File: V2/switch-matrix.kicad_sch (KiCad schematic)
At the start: 256 parts

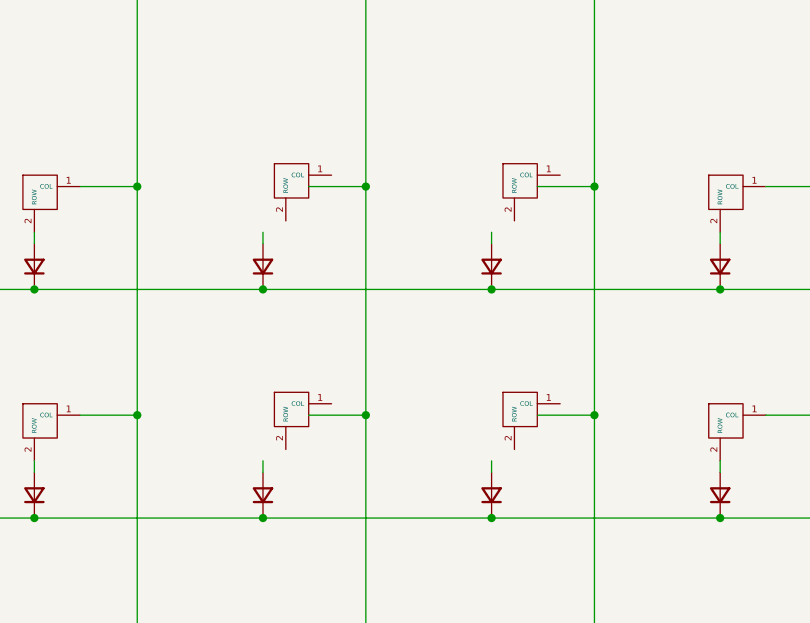
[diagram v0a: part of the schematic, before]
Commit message: Fixes + new files
Added RP2040 docs, fixed diodes in key matrix schematic, assigned RP2040 footprint to KiCAD stock QFN-56 7x7 package and made the BOOTSEL and RESET buttons smaller format.
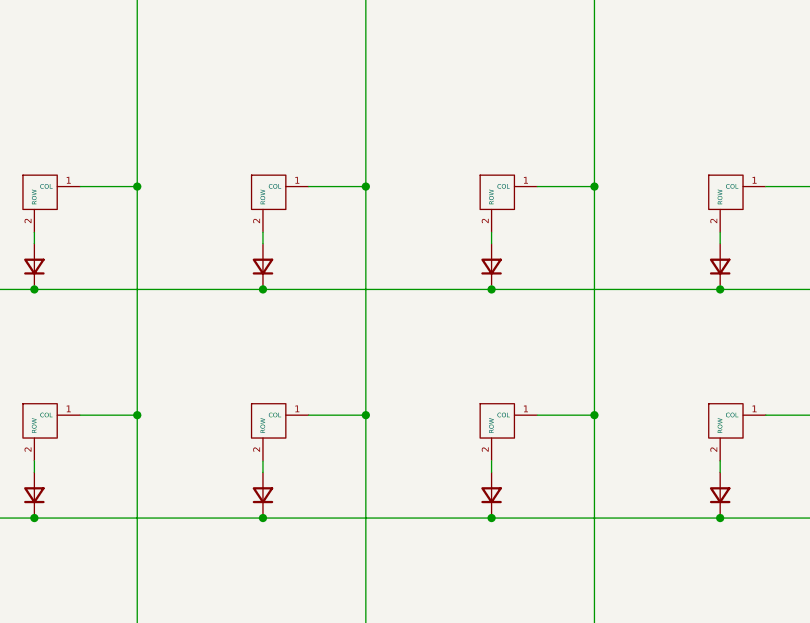
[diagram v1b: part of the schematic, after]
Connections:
- net col14: now also K_92.1 (COL), K_93.1 (COL)
- net col15: now also K_98.1 (COL), K_99.1 (COL)
- net at D_92.2 (A): now also K_92.2 (ROW)
- net at D_98.2 (A): now also K_98.2 (ROW)
- net at D_93.2 (A): now also K_93.2 (ROW)
- net at D_99.2 (A): now also K_99.2 (ROW)
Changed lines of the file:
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@@
 	)
 	(junction
+		(at 445.77 139.7)
+		(diameter 0)
+		(color 0 0 0 0)
+	)
+	(junction
 		(at 344.17 63.5)
 		(diameter 0)
@@
 	)
 	(junction
-		(at 445.77 139.7)
-		(diameter 0)
-		(color 0 0 0 0)
-	)
-	(junction
 		(at 535.94 74.93)
 		(diameter 0)
@@
 	(symbol
 		(lib_id "122-LIB:MX_Kailh_Hotswap_PnP")
-		(at 435.61 115.57 0)
+		(at 433.07 116.84 0)
 		(unit 1)
 		(body_style 1)
@@
 		(dnp no)
 		(property "Reference" "K_92"
-			(at 435.61 109.6518 0)
+			(at 433.07 110.9218 0)
 			(hide yes)
 			(show_name no)
@@
 		)
 		(property "Value" "KEYSW"
-			(at 435.61 118.11 0)
+			(at 433.07 119.38 0)
 			(hide yes)
 			(show_name no)
@@
 		)
 		(property "Footprint" "122-LIB:SW_Hotswap_Kailh_MX_1.00u_PnP"
-			(at 435.61 115.57 0)
+			(at 433.07 116.84 0)
 			(hide yes)
 			(show_name no)
@@
 		)
 		(property "Datasheet" ""
-			(at 435.61 115.57 0)
+			(at 433.07 116.84 0)
 			(hide yes)
 			(show_name no)
@@
 		)
 		(property "Description" ""
-			(at 435.61 115.57 0)
+			(at 433.07 116.84 0)
 			(hide yes)
 			(show_name no)
@@
 	(symbol
 		(lib_id "122-LIB:MX_Kailh_Hotswap_PnP")
-		(at 461.01 115.57 0)
+		(at 458.47 116.84 0)
 		(unit 1)
 		(body_style 1)
@@
 		(dnp no)
 		(property "Reference" "K_98"
-			(at 461.01 109.6518 0)
+			(at 458.47 110.9218 0)
 			(hide yes)
 			(show_name no)
@@
 		)
 		(property "Value" "KEYSW"
-			(at 461.01 118.11 0)
+			(at 458.47 119.38 0)
 			(hide yes)
 			(show_name no)
@@
 		)
 		(property "Footprint" "122-LIB:SW_Hotswap_Kailh_MX_1.00u_PnP"
-			(at 461.01 115.57 0)
+			(at 458.47 116.84 0)
 			(hide yes)
 			(show_name no)
@@
 		)
 		(property "Datasheet" ""
-			(at 461.01 115.57 0)
+			(at 458.47 116.84 0)
 			(hide yes)
 			(show_name no)
@@
 		)
 		(property "Description" ""
-			(at 461.01 115.57 0)
+			(at 458.47 116.84 0)
 			(hide yes)
 			(show_name no)
@@
 	(symbol
 		(lib_id "122-LIB:MX_Kailh_Hotswap_PnP")
-		(at 435.61 140.97 0)
+		(at 433.07 142.24 0)
 		(unit 1)
 		(body_style 1)
@@
 		(dnp no)
 		(property "Reference" "K_93"
-			(at 435.61 135.0518 0)
+			(at 433.07 136.3218 0)
 			(hide yes)
 			(show_name no)
@@
 		)
 		(property "Value" "KEYSW"
-			(at 435.61 143.51 0)
+			(at 433.07 144.78 0)
 			(hide yes)
 			(show_name no)
@@
 		)
 		(property "Footprint" "122-LIB:SW_Hotswap_Kailh_MX_1.00u_PnP"
-			(at 435.61 140.97 0)
+			(at 433.07 142.24 0)
 			(hide yes)
 			(show_name no)
@@
 		)
 		(property "Datasheet" ""
-			(at 435.61 140.97 0)
+			(at 433.07 142.24 0)
 			(hide yes)
 			(show_name no)
@@
 		)
 		(property "Description" ""
-			(at 435.61 140.97 0)
+			(at 433.07 142.24 0)
 			(hide yes)
 			(show_name no)
@@
 	(symbol
 		(lib_id "122-LIB:MX_Kailh_Hotswap_PnP")
-		(at 461.01 140.97 0)
+		(at 458.47 142.24 0)
 		(unit 1)
 		(body_style 1)
@@
 		(dnp no)
 		(property "Reference" "K_99"
-			(at 461.01 135.0518 0)
+			(at 458.47 136.3218 0)
 			(hide yes)
 			(show_name no)
@@
 		)
 		(property "Value" "KEYSW"
-			(at 461.01 143.51 0)
+			(at 458.47 144.78 0)
 			(hide yes)
 			(show_name no)
@@
 		)
 		(property "Footprint" "122-LIB:SW_Hotswap_Kailh_MX_1.00u_PnP"
-			(at 461.01 140.97 0)
+			(at 458.47 142.24 0)
 			(hide yes)
 			(show_name no)
@@
 		)
 		(property "Datasheet" ""
-			(at 461.01 140.97 0)
+			(at 458.47 142.24 0)
 			(hide yes)
 			(show_name no)
@@
 		)
 		(property "Description" ""
-			(at 461.01 140.97 0)
+			(at 458.47 142.24 0)
 			(hide yes)
 			(show_name no)

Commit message: Added PnP for plated thru holes + literature
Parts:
- K_1, K_128, K_94: footprint 122-LIB:SW_Hotswap_Kailh_MX_1.00u_PnP -> 122-LIB:SW_Hotswap_Kailh_MX_Plated_1.00u_PnP
- K_10: renamed from K_64; footprint 122-LIB:SW_Hotswap_Kailh_MX_1.00u_PnP -> 122-LIB:SW_Hotswap_Kailh_MX_Plated_1.00u_PnP
- K_100: renamed from K_5; footprint 122-LIB:SW_Hotswap_Kailh_MX_1.00u_PnP -> 122-LIB:SW_Hotswap_Kailh_MX_Plated_1.00u_PnP
- K_101: renamed from K_10; footprint 122-LIB:SW_Hotswap_Kailh_MX_1.00u_PnP -> 122-LIB:SW_Hotswap_Kailh_MX_Plated_1.00u_PnP
- K_102: renamed from K_16; footprint 122-LIB:SW_Hotswap_Kailh_MX_1.00u_PnP -> 122-LIB:SW_Hotswap_Kailh_MX_Plated_1.00u_PnP
- K_103: renamed from K_23; footprint 122-LIB:SW_Hotswap_Kailh_MX_1.00u_PnP -> 122-LIB:SW_Hotswap_Kailh_MX_Plated_1.00u_PnP
- K_104: renamed from K_29; footprint 122-LIB:SW_Hotswap_Kailh_MX_1.00u_PnP -> 122-LIB:SW_Hotswap_Kailh_MX_Plated_1.00u_PnP
- K_105: renamed from K_36; footprint 122-LIB:SW_Hotswap_Kailh_MX_1.00u_PnP -> 122-LIB:SW_Hotswap_Kailh_MX_Plated_1.00u_PnP
- K_106: renamed from K_43; footprint 122-LIB:SW_Hotswap_Kailh_MX_1.00u_PnP -> 122-LIB:SW_Hotswap_Kailh_MX_Plated_1.00u_PnP
- K_107: renamed from K_50; footprint 122-LIB:SW_Hotswap_Kailh_MX_1.00u_PnP -> 122-LIB:SW_Hotswap_Kailh_MX_Plated_1.00u_PnP
- K_108: renamed from K_57; footprint 122-LIB:SW_Hotswap_Kailh_MX_1.00u_PnP -> 122-LIB:SW_Hotswap_Kailh_MX_Plated_1.00u_PnP
- K_109: renamed from K_63; footprint 122-LIB:SW_Hotswap_Kailh_MX_1.00u_PnP -> 122-LIB:SW_Hotswap_Kailh_MX_Plated_1.00u_PnP
- K_11: renamed from K_71; footprint 122-LIB:SW_Hotswap_Kailh_MX_1.00u_PnP -> 122-LIB:SW_Hotswap_Kailh_MX_Plated_1.00u_PnP
- K_110: renamed from K_69; footprint 122-LIB:SW_Hotswap_Kailh_MX_1.00u_PnP -> 122-LIB:SW_Hotswap_Kailh_MX_Plated_1.00u_PnP
- K_111: renamed from K_76; footprint 122-LIB:SW_Hotswap_Kailh_MX_1.00u_PnP -> 122-LIB:SW_Hotswap_Kailh_MX_Plated_1.00u_PnP
- K_112: renamed from K_82; footprint 122-LIB:SW_Hotswap_Kailh_MX_1.00u_PnP -> 122-LIB:SW_Hotswap_Kailh_MX_Plated_1.00u_PnP
- K_113: renamed from K_88; footprint 122-LIB:SW_Hotswap_Kailh_MX_1.00u_PnP -> 122-LIB:SW_Hotswap_Kailh_MX_Plated_1.00u_PnP
- K_114: renamed from K_95; footprint 122-LIB:SW_Hotswap_Kailh_MX_1.00u_PnP -> 122-LIB:SW_Hotswap_Kailh_MX_Plated_1.00u_PnP
- K_115: renamed from K_101; footprint 122-LIB:SW_Hotswap_Kailh_MX_1.00u_PnP -> 122-LIB:SW_Hotswap_Kailh_MX_Plated_1.00u_PnP
- K_116: renamed from K_117; footprint 122-LIB:SW_Hotswap_Kailh_MX_1.00u_PnP -> 122-LIB:SW_Hotswap_Kailh_MX_Plated_1.00u_PnP
- K_117: renamed from K_6; footprint 122-LIB:SW_Hotswap_Kailh_MX_1.00u_PnP -> 122-LIB:SW_Hotswap_Kailh_MX_Plated_1.00u_PnP
- K_118: renamed from K_17; footprint 122-LIB:SW_Hotswap_Kailh_MX_1.00u_PnP -> 122-LIB:SW_Hotswap_Kailh_MX_Plated_1.00u_PnP
- K_119: renamed from K_30; footprint 122-LIB:SW_Hotswap_Kailh_MX_1.00u_PnP -> 122-LIB:SW_Hotswap_Kailh_MX_Plated_1.00u_PnP
- K_12: renamed from K_77; footprint 122-LIB:SW_Hotswap_Kailh_MX_1.00u_PnP -> 122-LIB:SW_Hotswap_Kailh_MX_Plated_1.00u_PnP
- K_120: renamed from K_37; footprint 122-LIB:SW_Hotswap_Kailh_MX_1.00u_PnP -> 122-LIB:SW_Hotswap_Kailh_MX_Plated_1.00u_PnP
- K_121: renamed from K_44; footprint 122-LIB:SW_Hotswap_Kailh_MX_1.00u_PnP -> 122-LIB:SW_Hotswap_Kailh_MX_Plated_1.00u_PnP
- K_122: renamed from K_51; footprint 122-LIB:SW_Hotswap_Kailh_MX_1.00u_PnP -> 122-LIB:SW_Hotswap_Kailh_MX_Plated_1.00u_PnP
- K_123: renamed from K_70; footprint 122-LIB:SW_Hotswap_Kailh_MX_1.00u_PnP -> 122-LIB:SW_Hotswap_Kailh_MX_Plated_1.00u_PnP
- K_124: renamed from K_89; footprint 122-LIB:SW_Hotswap_Kailh_MX_1.00u_PnP -> 122-LIB:SW_Hotswap_Kailh_MX_Plated_1.00u_PnP
- K_125: renamed from K_102; footprint 122-LIB:SW_Hotswap_Kailh_MX_1.00u_PnP -> 122-LIB:SW_Hotswap_Kailh_MX_Plated_1.00u_PnP
- K_126: renamed from K_118; footprint 122-LIB:SW_Hotswap_Kailh_MX_1.00u_PnP -> 122-LIB:SW_Hotswap_Kailh_MX_Plated_1.00u_PnP
- K_127: renamed from K_124; footprint 122-LIB:SW_Hotswap_Kailh_MX_1.00u_PnP -> 122-LIB:SW_Hotswap_Kailh_MX_Plated_1.00u_PnP
- K_13: renamed from K_83; footprint 122-LIB:SW_Hotswap_Kailh_MX_1.00u_PnP -> 122-LIB:SW_Hotswap_Kailh_MX_Plated_1.00u_PnP
- K_14: renamed from K_90; footprint 122-LIB:SW_Hotswap_Kailh_MX_1.00u_PnP -> 122-LIB:SW_Hotswap_Kailh_MX_Plated_1.00u_PnP
- K_15: renamed from K_96; footprint 122-LIB:SW_Hotswap_Kailh_MX_1.00u_PnP -> 122-LIB:SW_Hotswap_Kailh_MX_Plated_1.00u_PnP
- K_16: renamed from K_103; footprint 122-LIB:SW_Hotswap_Kailh_MX_1.00u_PnP -> 122-LIB:SW_Hotswap_Kailh_MX_Plated_1.00u_PnP
- K_17: renamed from K_108; footprint 122-LIB:SW_Hotswap_Kailh_MX_1.00u_PnP -> 122-LIB:SW_Hotswap_Kailh_MX_Plated_1.00u_PnP
- K_18: renamed from K_112; footprint 122-LIB:SW_Hotswap_Kailh_MX_1.00u_PnP -> 122-LIB:SW_Hotswap_Kailh_MX_Plated_1.00u_PnP
- K_19: renamed from K_119; footprint 122-LIB:SW_Hotswap_Kailh_MX_1.00u_PnP -> 122-LIB:SW_Hotswap_Kailh_MX_Plated_1.00u_PnP
- K_2: renamed from K_11; footprint 122-LIB:SW_Hotswap_Kailh_MX_1.00u_PnP -> 122-LIB:SW_Hotswap_Kailh_MX_Plated_1.00u_PnP
- K_20: renamed from K_12; footprint 122-LIB:SW_Hotswap_Kailh_MX_1.00u_PnP -> 122-LIB:SW_Hotswap_Kailh_MX_Plated_1.00u_PnP
- K_21: renamed from K_19; footprint 122-LIB:SW_Hotswap_Kailh_MX_1.00u_PnP -> 122-LIB:SW_Hotswap_Kailh_MX_Plated_1.00u_PnP
- K_22: renamed from K_25; footprint 122-LIB:SW_Hotswap_Kailh_MX_1.00u_PnP -> 122-LIB:SW_Hotswap_Kailh_MX_Plated_1.00u_PnP
- K_23: renamed from K_32; footprint 122-LIB:SW_Hotswap_Kailh_MX_1.00u_PnP -> 122-LIB:SW_Hotswap_Kailh_MX_Plated_1.00u_PnP
- K_24: renamed from K_39; footprint 122-LIB:SW_Hotswap_Kailh_MX_1.00u_PnP -> 122-LIB:SW_Hotswap_Kailh_MX_Plated_1.00u_PnP
- K_25: renamed from K_46; footprint 122-LIB:SW_Hotswap_Kailh_MX_1.00u_PnP -> 122-LIB:SW_Hotswap_Kailh_MX_Plated_1.00u_PnP
- K_26: renamed from K_53; footprint 122-LIB:SW_Hotswap_Kailh_MX_1.00u_PnP -> 122-LIB:SW_Hotswap_Kailh_MX_Plated_1.00u_PnP
- K_27: renamed from K_59; footprint 122-LIB:SW_Hotswap_Kailh_MX_1.00u_PnP -> 122-LIB:SW_Hotswap_Kailh_MX_Plated_1.00u_PnP
- K_28: renamed from K_65; footprint 122-LIB:SW_Hotswap_Kailh_MX_1.00u_PnP -> 122-LIB:SW_Hotswap_Kailh_MX_Plated_1.00u_PnP
- K_29: renamed from K_72; footprint 122-LIB:SW_Hotswap_Kailh_MX_1.00u_PnP -> 122-LIB:SW_Hotswap_Kailh_MX_Plated_1.00u_PnP
- K_3: renamed from K_18; footprint 122-LIB:SW_Hotswap_Kailh_MX_1.00u_PnP -> 122-LIB:SW_Hotswap_Kailh_MX_Plated_1.00u_PnP
- K_30: renamed from K_78; footprint 122-LIB:SW_Hotswap_Kailh_MX_1.00u_PnP -> 122-LIB:SW_Hotswap_Kailh_MX_Plated_1.00u_PnP
- K_31: renamed from K_84; footprint 122-LIB:SW_Hotswap_Kailh_MX_1.00u_PnP -> 122-LIB:SW_Hotswap_Kailh_MX_Plated_1.00u_PnP
- K_32: renamed from K_91; footprint 122-LIB:SW_Hotswap_Kailh_MX_1.00u_PnP -> 122-LIB:SW_Hotswap_Kailh_MX_Plated_1.00u_PnP
- K_33: renamed from K_97; footprint 122-LIB:SW_Hotswap_Kailh_MX_1.00u_PnP -> 122-LIB:SW_Hotswap_Kailh_MX_Plated_1.00u_PnP
- K_34: renamed from K_104; footprint 122-LIB:SW_Hotswap_Kailh_MX_1.00u_PnP -> 122-LIB:SW_Hotswap_Kailh_MX_Plated_1.00u_PnP
- K_35: renamed from K_109; footprint 122-LIB:SW_Hotswap_Kailh_MX_1.00u_PnP -> 122-LIB:SW_Hotswap_Kailh_MX_Plated_1.00u_PnP
- K_36: renamed from K_113; footprint 122-LIB:SW_Hotswap_Kailh_MX_1.00u_PnP -> 122-LIB:SW_Hotswap_Kailh_MX_Plated_1.00u_PnP
- K_37: renamed from K_120; footprint 122-LIB:SW_Hotswap_Kailh_MX_1.00u_PnP -> 122-LIB:SW_Hotswap_Kailh_MX_Plated_1.00u_PnP
- K_38: renamed from K_2; footprint 122-LIB:SW_Hotswap_Kailh_MX_1.00u_PnP -> 122-LIB:SW_Hotswap_Kailh_MX_Plated_1.00u_PnP
- K_39: renamed from K_7; footprint 122-LIB:SW_Hotswap_Kailh_MX_1.00u_PnP -> 122-LIB:SW_Hotswap_Kailh_MX_Plated_1.00u_PnP
- K_4: renamed from K_24; footprint 122-LIB:SW_Hotswap_Kailh_MX_1.00u_PnP -> 122-LIB:SW_Hotswap_Kailh_MX_Plated_1.00u_PnP
- K_40: renamed from K_13; footprint 122-LIB:SW_Hotswap_Kailh_MX_1.00u_PnP -> 122-LIB:SW_Hotswap_Kailh_MX_Plated_1.00u_PnP
- K_41: renamed from K_20; footprint 122-LIB:SW_Hotswap_Kailh_MX_1.00u_PnP -> 122-LIB:SW_Hotswap_Kailh_MX_Plated_1.00u_PnP
- K_42: renamed from K_26; footprint 122-LIB:SW_Hotswap_Kailh_MX_1.00u_PnP -> 122-LIB:SW_Hotswap_Kailh_MX_Plated_1.00u_PnP
- K_43: renamed from K_33; footprint 122-LIB:SW_Hotswap_Kailh_MX_1.00u_PnP -> 122-LIB:SW_Hotswap_Kailh_MX_Plated_1.00u_PnP
- K_44: renamed from K_40; footprint 122-LIB:SW_Hotswap_Kailh_MX_1.00u_PnP -> 122-LIB:SW_Hotswap_Kailh_MX_Plated_1.00u_PnP
- K_45: renamed from K_47; footprint 122-LIB:SW_Hotswap_Kailh_MX_1.00u_PnP -> 122-LIB:SW_Hotswap_Kailh_MX_Plated_1.00u_PnP
- K_46: renamed from K_54; footprint 122-LIB:SW_Hotswap_Kailh_MX_1.00u_PnP -> 122-LIB:SW_Hotswap_Kailh_MX_Plated_1.00u_PnP
- K_47: renamed from K_60; footprint 122-LIB:SW_Hotswap_Kailh_MX_1.00u_PnP -> 122-LIB:SW_Hotswap_Kailh_MX_Plated_1.00u_PnP
- K_48: renamed from K_66; footprint 122-LIB:SW_Hotswap_Kailh_MX_1.00u_PnP -> 122-LIB:SW_Hotswap_Kailh_MX_Plated_1.00u_PnP
- K_49: renamed from K_73; footprint 122-LIB:SW_Hotswap_Kailh_MX_1.00u_PnP -> 122-LIB:SW_Hotswap_Kailh_MX_Plated_1.00u_PnP
- K_5: renamed from K_31; footprint 122-LIB:SW_Hotswap_Kailh_MX_1.00u_PnP -> 122-LIB:SW_Hotswap_Kailh_MX_Plated_1.00u_PnP
- K_50: renamed from K_79; footprint 122-LIB:SW_Hotswap_Kailh_MX_1.00u_PnP -> 122-LIB:SW_Hotswap_Kailh_MX_Plated_1.00u_PnP
- K_51: renamed from K_85; footprint 122-LIB:SW_Hotswap_Kailh_MX_1.00u_PnP -> 122-LIB:SW_Hotswap_Kailh_MX_Plated_1.00u_PnP
- K_52: renamed from K_92; footprint 122-LIB:SW_Hotswap_Kailh_MX_1.00u_PnP -> 122-LIB:SW_Hotswap_Kailh_MX_Plated_1.00u_PnP
- K_53: renamed from K_98; footprint 122-LIB:SW_Hotswap_Kailh_MX_1.00u_PnP -> 122-LIB:SW_Hotswap_Kailh_MX_Plated_1.00u_PnP
- K_54: renamed from K_105; footprint 122-LIB:SW_Hotswap_Kailh_MX_1.00u_PnP -> 122-LIB:SW_Hotswap_Kailh_MX_Plated_1.00u_PnP
- K_55: renamed from K_110; footprint 122-LIB:SW_Hotswap_Kailh_MX_1.00u_PnP -> 122-LIB:SW_Hotswap_Kailh_MX_Plated_1.00u_PnP
- K_56: renamed from K_114; footprint 122-LIB:SW_Hotswap_Kailh_MX_1.00u_PnP -> 122-LIB:SW_Hotswap_Kailh_MX_Plated_1.00u_PnP
- K_57: renamed from K_121; footprint 122-LIB:SW_Hotswap_Kailh_MX_1.00u_PnP -> 122-LIB:SW_Hotswap_Kailh_MX_Plated_1.00u_PnP
- K_58: renamed from K_125; footprint 122-LIB:SW_Hotswap_Kailh_MX_1.00u_PnP -> 122-LIB:SW_Hotswap_Kailh_MX_Plated_1.00u_PnP
- K_59: renamed from K_3; footprint 122-LIB:SW_Hotswap_Kailh_MX_1.00u_PnP -> 122-LIB:SW_Hotswap_Kailh_MX_Plated_1.00u_PnP
- K_6: renamed from K_38; footprint 122-LIB:SW_Hotswap_Kailh_MX_1.00u_PnP -> 122-LIB:SW_Hotswap_Kailh_MX_Plated_1.00u_PnP
- K_60: renamed from K_8; footprint 122-LIB:SW_Hotswap_Kailh_MX_1.00u_PnP -> 122-LIB:SW_Hotswap_Kailh_MX_Plated_1.00u_PnP
- K_61: renamed from K_14; footprint 122-LIB:SW_Hotswap_Kailh_MX_1.00u_PnP -> 122-LIB:SW_Hotswap_Kailh_MX_Plated_1.00u_PnP
- K_62: renamed from K_21; footprint 122-LIB:SW_Hotswap_Kailh_MX_1.00u_PnP -> 122-LIB:SW_Hotswap_Kailh_MX_Plated_1.00u_PnP
- K_63: renamed from K_27; footprint 122-LIB:SW_Hotswap_Kailh_MX_1.00u_PnP -> 122-LIB:SW_Hotswap_Kailh_MX_Plated_1.00u_PnP
- K_64: renamed from K_34; footprint 122-LIB:SW_Hotswap_Kailh_MX_1.00u_PnP -> 122-LIB:SW_Hotswap_Kailh_MX_Plated_1.00u_PnP
- K_65: renamed from K_41; footprint 122-LIB:SW_Hotswap_Kailh_MX_1.00u_PnP -> 122-LIB:SW_Hotswap_Kailh_MX_Plated_1.00u_PnP
- K_66: renamed from K_48; footprint 122-LIB:SW_Hotswap_Kailh_MX_1.00u_PnP -> 122-LIB:SW_Hotswap_Kailh_MX_Plated_1.00u_PnP
- K_67: renamed from K_55; footprint 122-LIB:SW_Hotswap_Kailh_MX_1.00u_PnP -> 122-LIB:SW_Hotswap_Kailh_MX_Plated_1.00u_PnP
- K_68: renamed from K_61; footprint 122-LIB:SW_Hotswap_Kailh_MX_1.00u_PnP -> 122-LIB:SW_Hotswap_Kailh_MX_Plated_1.00u_PnP
- K_69: renamed from K_67; footprint 122-LIB:SW_Hotswap_Kailh_MX_1.00u_PnP -> 122-LIB:SW_Hotswap_Kailh_MX_Plated_1.00u_PnP
- K_7: renamed from K_45; footprint 122-LIB:SW_Hotswap_Kailh_MX_1.00u_PnP -> 122-LIB:SW_Hotswap_Kailh_MX_Plated_1.00u_PnP
- K_70: renamed from K_74; footprint 122-LIB:SW_Hotswap_Kailh_MX_1.00u_PnP -> 122-LIB:SW_Hotswap_Kailh_MX_Plated_1.00u_PnP
- K_71: renamed from K_80; footprint 122-LIB:SW_Hotswap_Kailh_MX_1.00u_PnP -> 122-LIB:SW_Hotswap_Kailh_MX_Plated_1.00u_PnP
- K_72: renamed from K_86; footprint 122-LIB:SW_Hotswap_Kailh_MX_1.00u_PnP -> 122-LIB:SW_Hotswap_Kailh_MX_Plated_1.00u_PnP
- K_73: renamed from K_93; footprint 122-LIB:SW_Hotswap_Kailh_MX_1.00u_PnP -> 122-LIB:SW_Hotswap_Kailh_MX_Plated_1.00u_PnP
- K_74: renamed from K_99; footprint 122-LIB:SW_Hotswap_Kailh_MX_1.00u_PnP -> 122-LIB:SW_Hotswap_Kailh_MX_Plated_1.00u_PnP
- K_75: renamed from K_106; footprint 122-LIB:SW_Hotswap_Kailh_MX_1.00u_PnP -> 122-LIB:SW_Hotswap_Kailh_MX_Plated_1.00u_PnP
- K_76: renamed from K_111; footprint 122-LIB:SW_Hotswap_Kailh_MX_1.00u_PnP -> 122-LIB:SW_Hotswap_Kailh_MX_Plated_1.00u_PnP
- K_77: renamed from K_115; footprint 122-LIB:SW_Hotswap_Kailh_MX_1.00u_PnP -> 122-LIB:SW_Hotswap_Kailh_MX_Plated_1.00u_PnP
- K_78: renamed from K_122; footprint 122-LIB:SW_Hotswap_Kailh_MX_1.00u_PnP -> 122-LIB:SW_Hotswap_Kailh_MX_Plated_1.00u_PnP
- K_79: renamed from K_126; footprint 122-LIB:SW_Hotswap_Kailh_MX_1.00u_PnP -> 122-LIB:SW_Hotswap_Kailh_MX_Plated_1.00u_PnP
- K_8: renamed from K_52; footprint 122-LIB:SW_Hotswap_Kailh_MX_1.00u_PnP -> 122-LIB:SW_Hotswap_Kailh_MX_Plated_1.00u_PnP
- K_80: renamed from K_4; footprint 122-LIB:SW_Hotswap_Kailh_MX_1.00u_PnP -> 122-LIB:SW_Hotswap_Kailh_MX_Plated_1.00u_PnP
- K_81: renamed from K_9; footprint 122-LIB:SW_Hotswap_Kailh_MX_1.00u_PnP -> 122-LIB:SW_Hotswap_Kailh_MX_Plated_1.00u_PnP
- K_82: renamed from K_15; footprint 122-LIB:SW_Hotswap_Kailh_MX_1.00u_PnP -> 122-LIB:SW_Hotswap_Kailh_MX_Plated_1.00u_PnP
- K_83: renamed from K_22; footprint 122-LIB:SW_Hotswap_Kailh_MX_1.00u_PnP -> 122-LIB:SW_Hotswap_Kailh_MX_Plated_1.00u_PnP
- K_84: renamed from K_28; footprint 122-LIB:SW_Hotswap_Kailh_MX_1.00u_PnP -> 122-LIB:SW_Hotswap_Kailh_MX_Plated_1.00u_PnP
- K_85: renamed from K_35; footprint 122-LIB:SW_Hotswap_Kailh_MX_1.00u_PnP -> 122-LIB:SW_Hotswap_Kailh_MX_Plated_1.00u_PnP
- K_86: renamed from K_42; footprint 122-LIB:SW_Hotswap_Kailh_MX_1.00u_PnP -> 122-LIB:SW_Hotswap_Kailh_MX_Plated_1.00u_PnP
- K_87: renamed from K_49; footprint 122-LIB:SW_Hotswap_Kailh_MX_1.00u_PnP -> 122-LIB:SW_Hotswap_Kailh_MX_Plated_1.00u_PnP
- K_88: renamed from K_56; footprint 122-LIB:SW_Hotswap_Kailh_MX_1.00u_PnP -> 122-LIB:SW_Hotswap_Kailh_MX_Plated_1.00u_PnP
- K_89: renamed from K_62; footprint 122-LIB:SW_Hotswap_Kailh_MX_1.00u_PnP -> 122-LIB:SW_Hotswap_Kailh_MX_Plated_1.00u_PnP
- K_9: renamed from K_58; footprint 122-LIB:SW_Hotswap_Kailh_MX_1.00u_PnP -> 122-LIB:SW_Hotswap_Kailh_MX_Plated_1.00u_PnP
- K_90: renamed from K_68; footprint 122-LIB:SW_Hotswap_Kailh_MX_1.00u_PnP -> 122-LIB:SW_Hotswap_Kailh_MX_Plated_1.00u_PnP
- K_91: renamed from K_75; footprint 122-LIB:SW_Hotswap_Kailh_MX_1.00u_PnP -> 122-LIB:SW_Hotswap_Kailh_MX_Plated_1.00u_PnP
- K_92: renamed from K_81; footprint 122-LIB:SW_Hotswap_Kailh_MX_1.00u_PnP -> 122-LIB:SW_Hotswap_Kailh_MX_Plated_1.00u_PnP
- K_93: renamed from K_87; footprint 122-LIB:SW_Hotswap_Kailh_MX_1.00u_PnP -> 122-LIB:SW_Hotswap_Kailh_MX_Plated_1.00u_PnP
- K_95: renamed from K_100; footprint 122-LIB:SW_Hotswap_Kailh_MX_1.00u_PnP -> 122-LIB:SW_Hotswap_Kailh_MX_Plated_1.00u_PnP
- K_96: renamed from K_107; footprint 122-LIB:SW_Hotswap_Kailh_MX_1.00u_PnP -> 122-LIB:SW_Hotswap_Kailh_MX_Plated_1.00u_PnP
- K_97: renamed from K_116; footprint 122-LIB:SW_Hotswap_Kailh_MX_1.00u_PnP -> 122-LIB:SW_Hotswap_Kailh_MX_Plated_1.00u_PnP
- K_98: renamed from K_123; footprint 122-LIB:SW_Hotswap_Kailh_MX_1.00u_PnP -> 122-LIB:SW_Hotswap_Kailh_MX_Plated_1.00u_PnP
- K_99: renamed from K_127; footprint 122-LIB:SW_Hotswap_Kailh_MX_1.00u_PnP -> 122-LIB:SW_Hotswap_Kailh_MX_Plated_1.00u_PnP
- renumbered D_64 to D_10, D_5 to D_100, D_10 to D_101, D_16 to D_102, D_23 to D_103, D_29 to D_104, D_36 to D_105, D_43 to D_106, D_50 to D_107, D_57 to D_108, D_63 to D_109, D_71 to D_11, D_69 to D_110, D_76 to D_111, D_82 to D_112, D_88 to D_113, D_95 to D_114, D_101 to D_115, D_117 to D_116, D_6 to D_117, D_17 to D_118, D_30 to D_119, D_77 to D_12, D_37 to D_120, D_44 to D_121, D_51 to D_122, D_70 to D_123, D_89 to D_124, D_102 to D_125, D_118 to D_126, D_124 to D_127, D_83 to D_13, D_90 to D_14, D_96 to D_15, D_103 to D_16, D_108 to D_17, D_112 to D_18, D_119 to D_19, D_11 to D_2, D_12 to D_20, D_19 to D_21, D_25 to D_22, D_32 to D_23, D_39 to D_24, D_46 to D_25, D_53 to D_26, D_59 to D_27, D_65 to D_28, D_72 to D_29, D_18 to D_3, D_78 to D_30, D_84 to D_31, D_91 to D_32, D_97 to D_33, D_104 to D_34, D_109 to D_35, D_113 to D_36, D_120 to D_37, D_2 to D_38, D_7 to D_39, D_24 to D_4, D_13 to D_40, D_20 to D_41, D_26 to D_42, D_33 to D_43, D_40 to D_44, D_47 to D_45, D_54 to D_46, D_60 to D_47, D_66 to D_48, D_73 to D_49, D_31 to D_5, D_79 to D_50, D_85 to D_51, D_92 to D_52, D_98 to D_53, D_105 to D_54, D_110 to D_55, D_114 to D_56, D_121 to D_57, D_125 to D_58, D_3 to D_59, D_38 to D_6, D_8 to D_60, D_14 to D_61, D_21 to D_62, D_27 to D_63, D_34 to D_64, D_41 to D_65, D_48 to D_66, D_55 to D_67, D_61 to D_68, D_67 to D_69, D_45 to D_7, D_74 to D_70, D_80 to D_71, D_86 to D_72, D_93 to D_73, D_99 to D_74, D_106 to D_75, D_111 to D_76, D_115 to D_77, D_122 to D_78, D_126 to D_79, D_52 to D_8, D_4 to D_80, D_9 to D_81, D_15 to D_82, D_22 to D_83, D_28 to D_84, D_35 to D_85, D_42 to D_86, D_49 to D_87, D_56 to D_88, D_62 to D_89, D_58 to D_9, D_68 to D_90, D_75 to D_91, D_81 to D_92, D_87 to D_93, D_100 to D_95, D_107 to D_96, D_116 to D_97, D_123 to D_98, D_127 to D_99

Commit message: Updated KiCad Files
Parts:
- added FID1, FID2, FID3: Fiducial, Fiducial:Fiducial_1mm_Mask2mm, symbol Mechanical:Fiducial
- D_1, D_10, D_100, D_101, D_102, D_103, D_104, D_105, D_106, D_107, D_108, D_109, D_11, D_110, D_111, D_112, D_113, D_114, D_115, D_116, D_117, D_118, D_119, D_12, D_120, D_121, D_122, D_123, D_124, D_125, D_126, D_127, D_128, D_13, D_14, D_15, D_16, D_17, D_18, D_19, D_2, D_20, D_21, D_22, D_23, D_24, D_25, D_26, D_27, D_28, D_29, D_3, D_30, D_31, D_32, D_33, D_34, D_35, D_36, D_37, D_38, D_39, D_4, D_40, D_41, D_42, D_43, D_44, D_45, D_46, D_47, D_48, D_49, D_5, D_50, D_51, D_52, D_53, D_54, D_55, D_56, D_57, D_58, D_59, D_6, D_60, D_61, D_62, D_63, D_64, D_65, D_66, D_67, D_68, D_69, D_7, D_70, D_71, D_72, D_73, D_74, D_75, D_76, D_77, D_78, D_79, D_8, D_80, D_81, D_82, D_83, D_84, D_85, D_86, D_87, D_88, D_89, D_9, D_90, D_91, D_92, D_93, D_94, D_95, D_96, D_97, D_98, D_99: LCSC Part Number (none) -> C963381
- K_1, K_10, K_100, K_101, K_102, K_103, K_104, K_105, K_106, K_107, K_108, K_109, K_11, K_110, K_111, K_112, K_113, K_114, K_115, K_116, K_117, K_118, K_119, K_12, K_120, K_121, K_122, K_123, K_124, K_125, K_126, K_127, K_128, K_13, K_14, K_15, K_16, K_17, K_18, K_19, K_2, K_20, K_21, K_22, K_23, K_24, K_25, K_26, K_27, K_28, K_29, K_3, K_30, K_31, K_32, K_33, K_34, K_35, K_36, K_37, K_38, K_39, K_4, K_40, K_41, K_42, K_43, K_44, K_45, K_46, K_47, K_48, K_49, K_5, K_50, K_51, K_52, K_53, K_54, K_55, K_56, K_57, K_58, K_59, K_6, K_60, K_61, K_62, K_63, K_64, K_65, K_66, K_67, K_68, K_69, K_7, K_70, K_71, K_72, K_73, K_74, K_75, K_76, K_77, K_78, K_79, K_8, K_80, K_81, K_82, K_83, K_84, K_85, K_86, K_87, K_88, K_89, K_9, K_90, K_91, K_92, K_93, K_94, K_95, K_96, K_97, K_98, K_99: LCSC Part Number (none) -> C41430893
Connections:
- net col4: now also K_22.1 (COL)
